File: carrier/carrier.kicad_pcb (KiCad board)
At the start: 4 copper layers, 9.2 x 7.4 mm, 2 parts, among them J1 DF40TC-30DP-0.4V(51), U1 TC58NVG1S3HBAI6

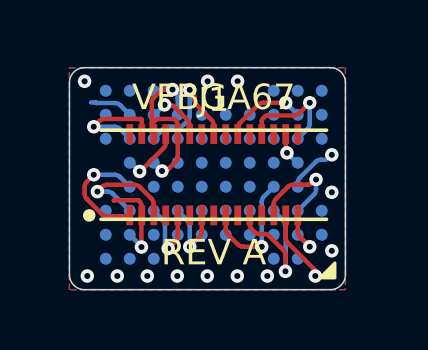
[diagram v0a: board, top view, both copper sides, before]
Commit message: Snapshot Courk-style unrouted NAND interposer
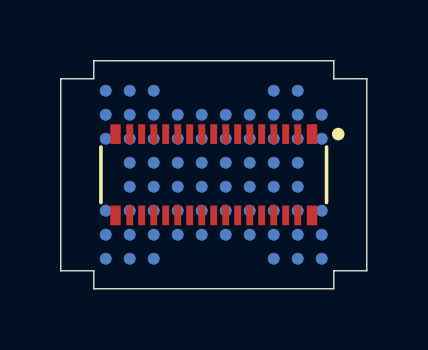
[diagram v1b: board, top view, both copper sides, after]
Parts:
- J1: footprint Connector_Hirose_DF40:HIROSE_DF40TC-30DP-0.4V_51_ -> HIROSE_DF40TC-30DP-0.4V_51_
- U1: value TC58NVG1S3HBAI6 -> HOME_VFBGA67_INTERFACE; footprint carrier:BGA-67_6.5x8.0mm_Layout8x10_P0.8mm -> carrier:BGA-67_6.5x8.0mm_Layout8x10_P0.8mm_Mirrored_Interposer
- turned J1 to 180 degrees
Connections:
- J1 pad 1: /IO4 -> GND
- J1 pad 10: VCC -> //WP
- J1 pad 11: GND -> //CE
- J1 pad 12: /IO8 -> //RE
- J1 pad 13: /IO1 -> /CLE
- J1 pad 14: GND -> VCC
- J1 pad 16: /IO6 -> GND
- J1 pad 17: /CLE -> GND
- J1 pad 18: GND -> /IO5
- J1 pad 20: /RY//BY -> /IO2
- J1 pad 21: //RE -> /IO6
- J1 pad 22: GND -> /IO1
- J1 pad 23: GND -> /IO8
- J1 pad 24: //WE -> /IO3
- J1 pad 25: /ALE -> /IO7
- J1 pad 26: GND -> /IO4
- J1 pad 28: //CE -> GND
- J1 pad 29: //WP -> GND
- J1 pad 4: /IO7 -> GND
- J1 pad 5: /IO3 -> GND
- J1 pad 6: VCC -> GND
- J1 pad 7: GND -> /RY//BY
- J1 pad 8: /IO5 -> /ALE
- J1 pad 9: /IO2 -> //WE
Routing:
- net GND: track 8.23 -> 0.00 mm, vias 15 -> 0
- net VCC: track 6.21 -> 0.00 mm, vias 2 -> 0
- net //RE: track 4.70 -> 0.00 mm, vias 1 -> 0
- net /IO6: track 4.17 -> 0.00 mm, vias 1 -> 0
- net /CLE: track 4.09 -> 0.00 mm, vias 1 -> 0
- net /IO3: track 3.97 -> 0.00 mm, vias 1 -> 0
- net /IO4: track 3.96 -> 0.00 mm, vias 1 -> 0
- net //WE: track 3.65 -> 0.00 mm, vias 1 -> 0
- net /IO7: track 3.54 -> 0.00 mm, vias 1 -> 0
- net /ALE: track 3.43 -> 0.00 mm, vias 1 -> 0
- net /RY//BY: track 2.75 -> 0.00 mm, vias 1 -> 0
- net /IO2: track 2.66 -> 0.00 mm, vias 1 -> 0
- net /IO1: track 2.55 -> 0.00 mm, vias 1 -> 0
- net /IO5: track 2.06 -> 0.00 mm, vias 1 -> 0
- net /IO8: track 1.95 -> 0.00 mm, vias 1 -> 0
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- removed copper zone on B.Cu, net GND
- removed copper zone on F.Cu, net GND
- removed copper zone on In1.Cu, net GND
- removed copper zone on In2.Cu, net GND
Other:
- board size 9.2 x 7.4 mm -> 10.2 x 7.6 mm
- board text removed: "REV A"
- board text removed: "VFBGA67"

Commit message: Route carrier board
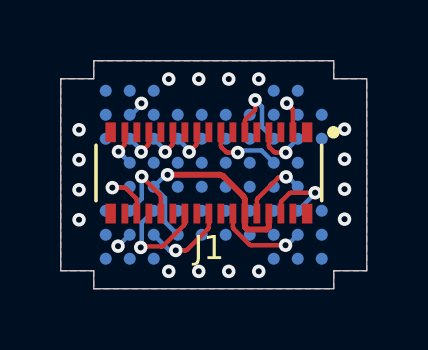
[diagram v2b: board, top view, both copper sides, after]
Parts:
- J1: footprint HIROSE_DF40TC-30DP-0.4V_51_ -> Connector_Hirose_DF40:HIROSE_DF40TC-30DP-0.4V_51_
- moved J1 0.17 mm to (168.4, 85.5)
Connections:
- J1 pad 1: GND -> //WP
- J1 pad 10: //WP -> VCC
- J1 pad 11: //CE -> GND
- J1 pad 12: //RE -> /RY//BY
- J1 pad 14: VCC -> GND
- J1 pad 16: GND -> /IO8
- J1 pad 17: GND -> /IO1
- J1 pad 18: /IO5 -> GND
- J1 pad 20: /IO2 -> /IO6
- J1 pad 21: /IO6 -> /IO2
- J1 pad 22: /IO1 -> GND
- J1 pad 23: /IO8 -> GND
- J1 pad 24: /IO3 -> /IO7
- J1 pad 25: /IO7 -> /IO3
- J1 pad 26: /IO4 -> GND
- J1 pad 28: GND -> /IO5
- J1 pad 29: GND -> /IO4
- J1 pad 4: GND -> //WE
- J1 pad 5: GND -> /ALE
- J1 pad 6: GND -> VCC
- J1 pad 7: /RY//BY -> GND
- J1 pad 8: /ALE -> //CE
- J1 pad 9: //WE -> //RE
- J1 pad MT1: (no net) -> GND
- J1 pad MT2: (no net) -> GND
- J1 pad MT3: (no net) -> GND
- J1 pad MT4: (no net) -> GND
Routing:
- net VCC: track 0.00 -> 7.72 mm, vias 0 -> 1
- net /IO6: track 0.00 -> 3.54 mm, vias 0 -> 1
- net /RY//BY: track 0.00 -> 3.02 mm, vias 0 -> 1
- net /IO8: track 0.00 -> 2.83 mm, vias 0 -> 1
- net /IO7: track 0.00 -> 2.80 mm, vias 0 -> 1
- net //RE: track 0.00 -> 2.76 mm, vias 0 -> 1
- net /CLE: track 0.00 -> 2.51 mm, vias 0 -> 1
- net //WE: track 0.00 -> 2.49 mm, vias 0 -> 1
- net //CE: track 0.00 -> 2.28 mm, vias 0 -> 1
- net /IO5: track 0.00 -> 2.04 mm, vias 0 -> 1
- net /ALE: track 0.00 -> 1.74 mm, vias 0 -> 1
- net //WP: track 0.00 -> 1.59 mm, vias 0 -> 1
- net /IO2: track 0.00 -> 1.35 mm, vias 0 -> 1
- net /IO3: track 0.00 -> 1.35 mm, vias 0 -> 1
- net /IO1: track 0.00 -> 1.35 mm, vias 0 -> 1
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- added copper zone on B.Cu, net GND
- added copper zone on F.Cu, net GND
- added copper zone on In1.Cu, net GND
- added copper zone on In2.Cu, net GND
